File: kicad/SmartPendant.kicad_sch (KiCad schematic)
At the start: 56 parts, among them J1 UART, J2 ST-LINK, J3 Conn_01x05, J4 TYPE-C16PIN, J5 Conn_01x14, P2 KH-FG0.5-H2.0-6PIN, Q1 MMBT3904, U2 AMS1117-3.3, U3 MB85RC256VPNF

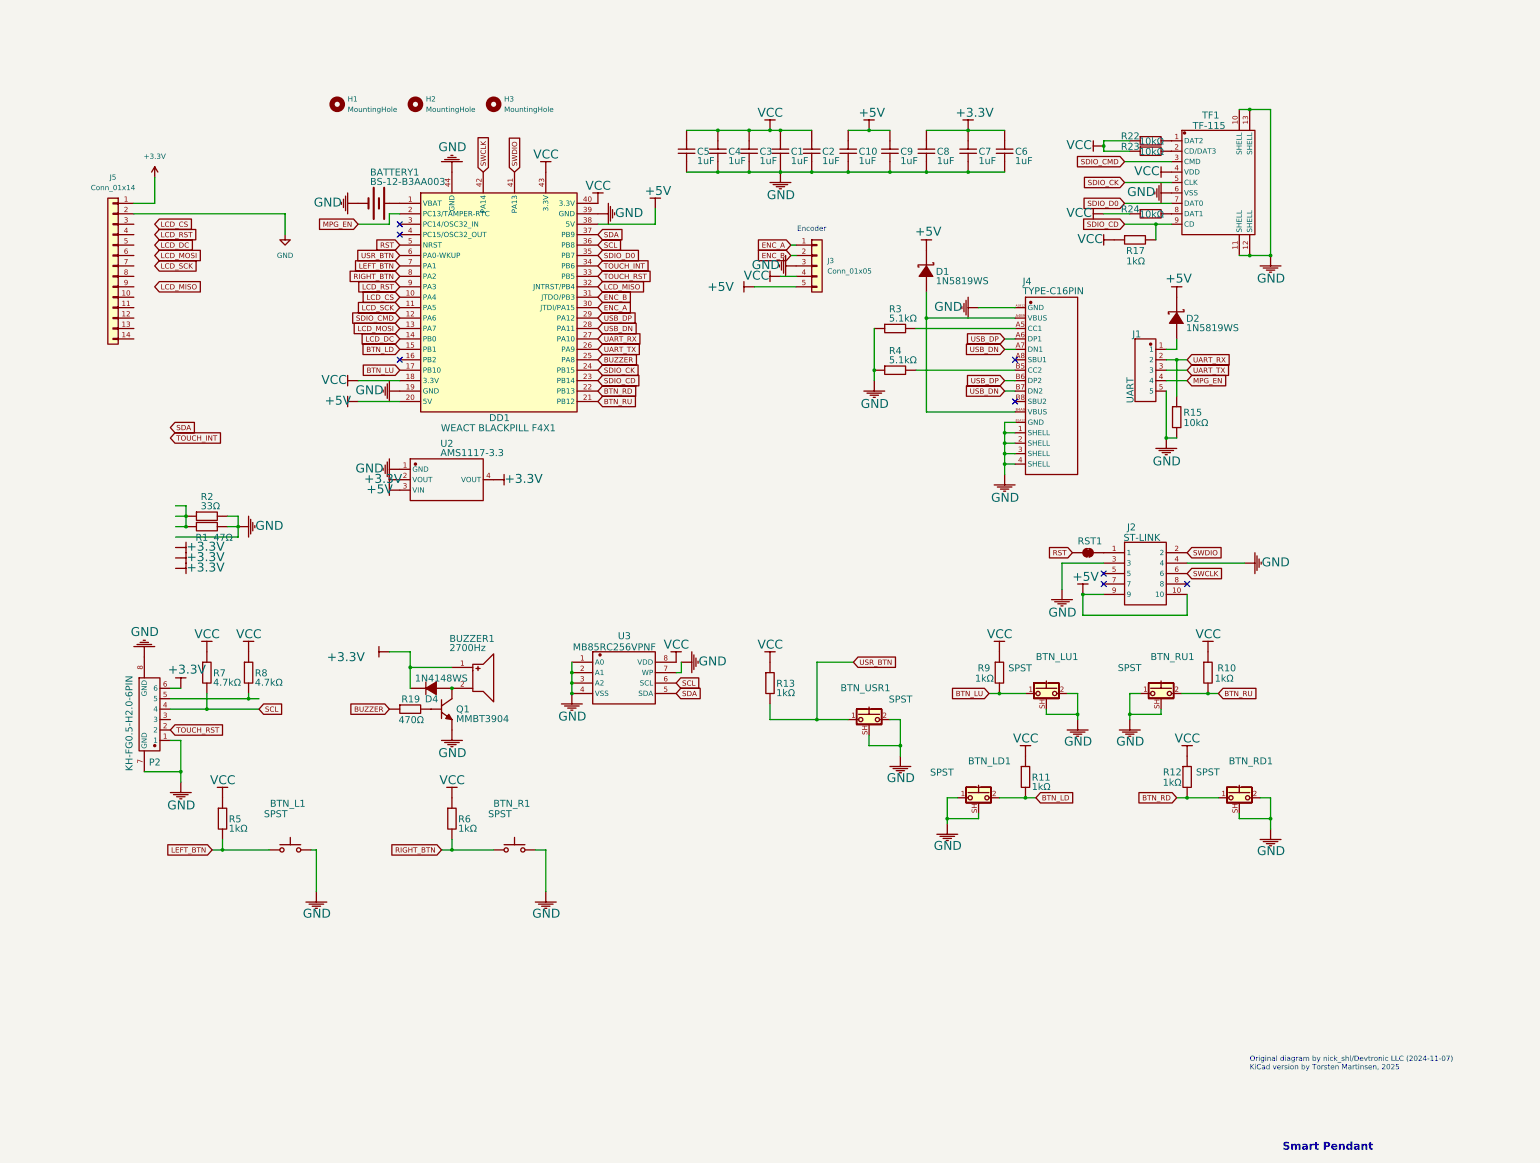
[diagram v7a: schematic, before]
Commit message: Change most symbols to proper KiCad ones.
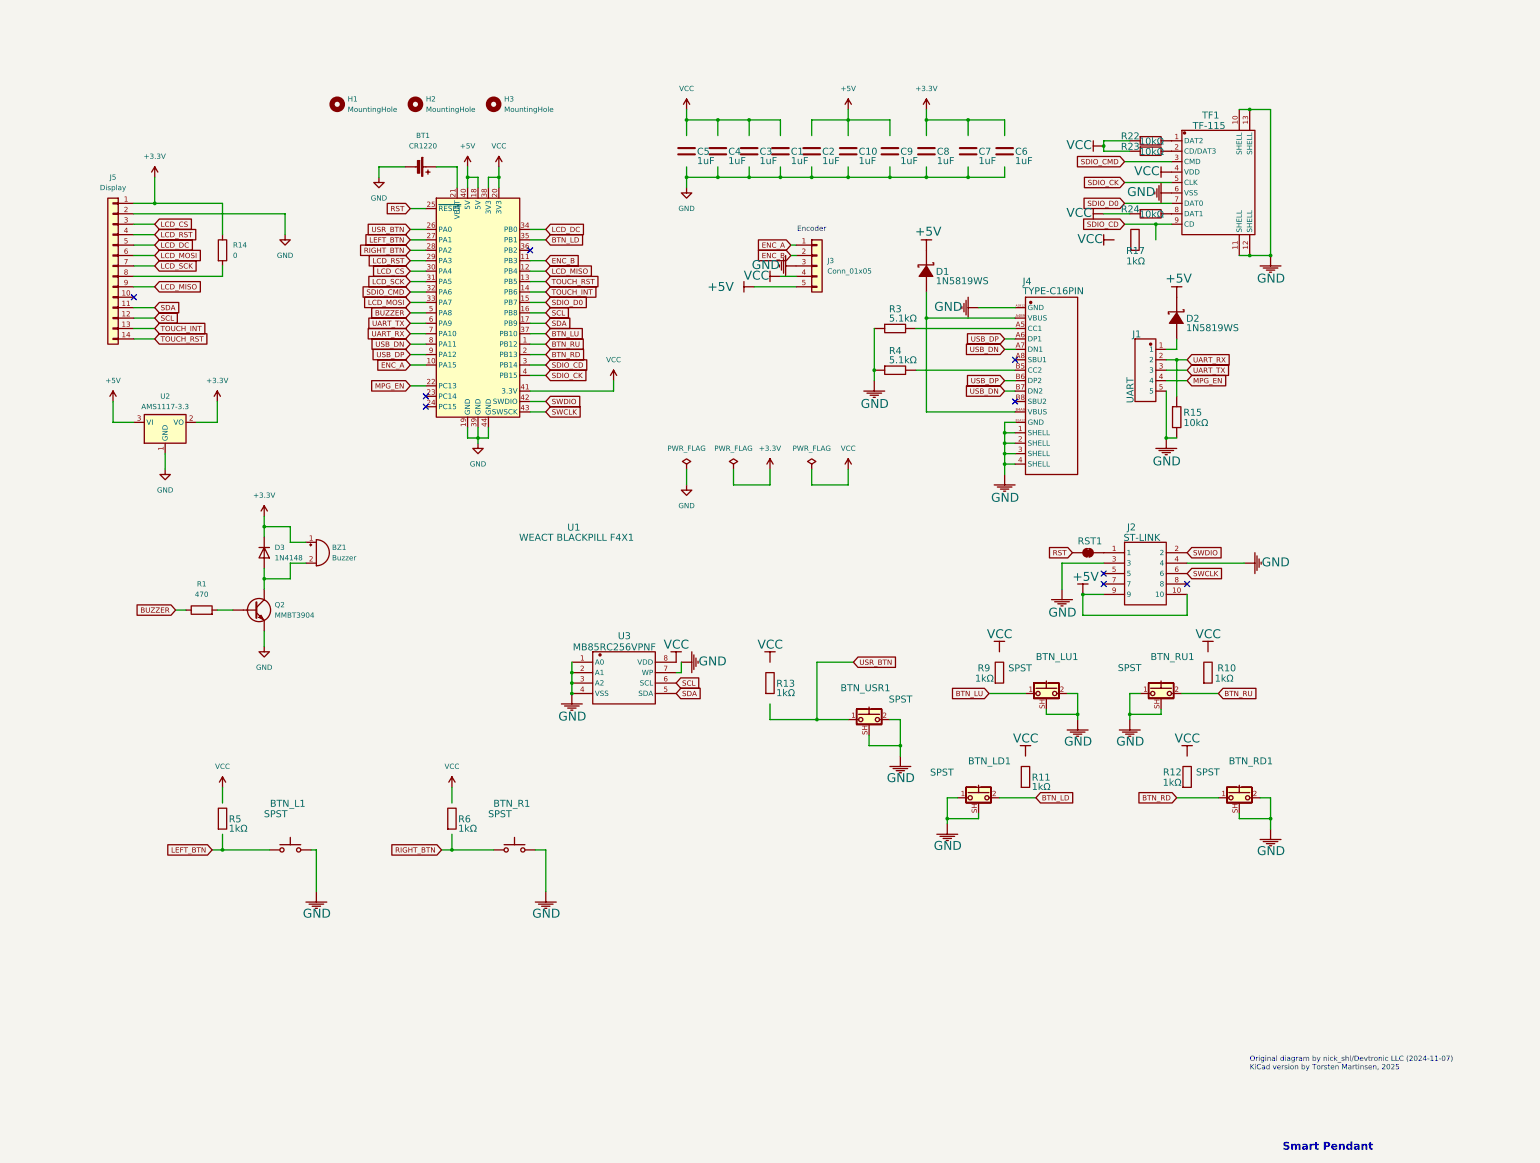
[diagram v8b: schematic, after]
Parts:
- removed BATTERY1: BS-12-B3AA003, Battery:BatteryHolder_Keystone_1060_1x2032, symbol BS-12-B3AA003
- removed BUZZER1: 2700Hz, symbol QMB-09B-03
- removed D4: 1N4148WS, PCM_Diode_SMD_AKL:D_MiniMELF, symbol 1N4148WS T4
- removed P2: KH-FG0.5-H2.0-6PIN, symbol KH-FG0.5-H2.0-6PIN
- removed Q1: MMBT3904, PCM_Package_TO_SOT_SMD_AKL:SOT-23, symbol SS8050_C2150
- removed R1: 47Ω, PCM_Resistor_SMD_AKL:R_0603_1608Metric, symbol 0805W8F470JT5E
- removed R19: 470Ω, PCM_Resistor_SMD_AKL:R_0603_1608Metric, symbol 0805W8F4700T5E
- removed R2: 33Ω, PCM_Resistor_SMD_AKL:R_0603_1608Metric, symbol 0805W8F330JT5E
- removed R7: 4.7kΩ, PCM_Resistor_SMD_AKL:R_0603_1608Metric, symbol 0805W8F1002T5E_7
- removed R8: 4.7kΩ, PCM_Resistor_SMD_AKL:R_0603_1608Metric, symbol 0805W8F1002T5E_6
- removed U2: AMS1117-3.3, PCM_Package_TO_SOT_SMD_AKL:SOT-223, symbol AMS1117-3.3
- added BT1: CR1220, symbol Device:Battery_Cell
- added BZ1: Buzzer, symbol Device:Buzzer
- added D3: 1N4148, PCM_Diode_SMD_AKL:D_MiniMELF, symbol Device:D
- added Q2: MMBT3904, symbol Device:Q_NPN
- added R1: 470, PCM_Resistor_SMD_AKL:R_0603_1608Metric, symbol Device:R
- added R14: 0, PCM_Resistor_SMD_AKL:R_0603_1608Metric, symbol Device:R
- added U2: AMS1117-3.3, PCM_Package_TO_SOT_SMD_AKL:SOT-223-3_TabPin2, symbol Regulator_Linear:AMS1117-3.3
- BTN_L1, BTN_R1: footprint (none) -> Button_Switch_SMD:SW_Push_1P1T_XKB_TS-1187A
- C1: symbol TCC0805X7R105M500FT -> Device:C
- C10: symbol TCC0805X7R105M500FT_8 -> Device:C
- C2: symbol TCC0805X7R105M500FT_1 -> Device:C
- C3: symbol TCC0805X7R105M500FT_5 -> Device:C
- C4: symbol TCC0805X7R105M500FT_6 -> Device:C
- C5: symbol TCC0805X7R105M500FT_7 -> Device:C
- C6: symbol TCC0805X7R105M500FT_4 -> Device:C
- C7: symbol TCC0805X7R105M500FT_3 -> Device:C
- C8: symbol TCC0805X7R105M500FT_9 -> Device:C
- C9: symbol TCC0805X7R105M500FT_2 -> Device:C
- J4: footprint (none) -> Custom:USB_C_Receptacle_AliExpress_16pin
- J5: value Conn_01x14 -> Display; footprint (none) -> Connector_PinSocket_2.54mm:PinSocket_1x14_P2.54mm_Vertical_SMD_Pin1Left
- R10: symbol 0805W8F1002T5E_3 -> Device:R
- R11: symbol 0805W8F1002T5E_4 -> Device:R
- R12: symbol 0805W8F1002T5E_5 -> Device:R
- R13: symbol 0805W8F1002T5E_10 -> Device:R
- R17: symbol 0805W8F1002T5E_11 -> Device:R
- R5: symbol 0805W8F1002T5E -> Device:R
- R6: symbol 0805W8F1002T5E_1 -> Device:R
- R9: symbol 0805W8F1002T5E_2 -> Device:R
- U1: renamed from DD1; footprint (none) -> Custom:BlackPill_STLINK; symbol WEACT BLACKPILL F4X1 -> blackpill_stlink:BlackPill_STLINK
- U3: footprint (none) -> PCM_Package_SO_AKL:SOP-8_3.9x4.9mm_P1.27mm
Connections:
- net +3.3V: now also BZ1.1 (+), D3.1 (K), R14.1, U2.2 (VO); no longer C6.2, C7.2, C8.2
- net +5V: now also U1.18 (5V), U1.40 (5V), U2.3 (VI); no longer C10.2, C9.2, U1.20 (5V), U1.38 (5V)
- net BTN_LD: now also U1.35 (PB1); no longer R11.2, U1.15 (PB1)
- net BTN_LU: now also U1.37 (PB10); no longer R9.2, U1.17 (PB10)
- net BTN_RD: now also U1.2 (PB13); no longer R12.2, U1.22 (PB13)
- net BTN_RU: now also U1.1 (PB12); no longer R10.2, U1.21 (PB12)
- net BUZZER: now also U1.5 (PA8), R1.1; no longer U1.25 (PA8)
- net ENC_A: now also U1.10 (PA15); no longer U1.30 (JTDI/PA15)
- net ENC_B: now also U1.11 (PB3); no longer U1.31 (JTDO/PB3)
- net GND: now also BT1.2 (-), Q2.E, U2.1 (GND); no longer C1.1, C10.1, C2.1, C3.1, C4.1, C5.1, C6.1, C7.1, C8.1, C9.1
- net LCD_CS: now also J5.3 (Pin_3), U1.30 (PA4); no longer U1.10 (PA4)
- net LCD_DC: now also J5.5 (Pin_5), U1.34 (PB0); no longer U1.14 (PB0)
- net LCD_MISO: now also J5.9 (Pin_9), U1.12 (PB4); no longer U1.32 (JNTRST/PB4)
- net LCD_MOSI: now also J5.6 (Pin_6), U1.33 (PA7); no longer U1.13 (PA7)
- net LCD_RST: now also J5.4 (Pin_4), U1.29 (PA3); no longer U1.9 (PA3)
- net LCD_SCK: now also J5.7 (Pin_7), U1.31 (PA5); no longer U1.11 (PA5)
- net LEFT_BTN: now also U1.27 (PA1); no longer R5.2, U1.7 (PA1)
- net MPG_EN: now also U1.22 (PC13); no longer U1.2 (PC13/TAMPER-RTC)
- net RIGHT_BTN: now also U1.28 (PA2); no longer R6.2, U1.8 (PA2)
- net RST: now also U1.25 (~{RESET}); no longer U1.5 (NRST)
- net SCL: now also J5.12 (Pin_12), U1.16 (PB8); no longer U1.36 (PB8)
- net SDA: now also J5.11 (Pin_11), U1.17 (PB9); no longer U1.37 (PB9)
- net SDIO_CD: now also U1.3 (PB14); no longer R17.2, U1.23 (PB14)
- net SDIO_CK: now also U1.4 (PB15); no longer U1.24 (PB15)
- net SDIO_CMD: now also U1.32 (PA6); no longer U1.12 (PA6)
- net SDIO_D0: now also U1.15 (PB7); no longer U1.35 (PB7)
- net SWCLK: now also U1.43 (SWSCK); no longer U1.42 (PA14)
- net SWDIO: now also U1.42 (SWDIO); no longer U1.41 (PA13)
- net TOUCH_INT: now also J5.13 (Pin_13), U1.14 (PB6); no longer U1.34 (PB6)
- net TOUCH_RST: now also J5.14 (Pin_14), U1.13 (PB5); no longer U1.33 (PB5)
- net UART_RX: now also U1.7 (PA10); no longer U1.27 (PA10)
- net UART_TX: now also U1.6 (PA9); no longer U1.26 (PA9)
- net USB_DN: now also U1.8 (PA11); no longer U1.28 (PA11)
- net USB_DP: now also U1.9 (PA12); no longer U1.29 (PA12)
- net USR_BTN: now also U1.26 (PA0); no longer R13.2, U1.6 (PA0-WKUP)
- net VCC: now also U1.20 (3V3), U1.38 (3V3), U1.41 (3.3V); no longer C1.2, C2.2, C3.2, C4.2, C5.2, R10.1, R11.1, R12.1, R13.1, R17.1, R5.1, R6.1, R9.1, U1.18 (3.3V), U1.40 (3.3V), U1.43 (3.3V)
- net at J5.8 (Pin_8): now also R14.2
- new net: Q2.B, R1.2
- new net: BZ1.2 (-), D3.2 (A), Q2.C
- new net: BT1.1 (+), U1.21 (VBAT)
- no-connect marks 8 -> 9
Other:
- moved on the sheet: U1
